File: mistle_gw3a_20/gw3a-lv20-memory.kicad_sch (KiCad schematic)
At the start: 9 parts, among them U13 MT48LC16M16A2TG, U6 W25Q128JVS

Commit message: Update gw3a dev board
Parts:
- added D6, D7: green, LED_SMD:LED_0805_2012Metric, symbol Device:LED
- added R13, R14, R35: 330, Resistor_SMD:R_0402_1005Metric, symbol Device:R_Small
- added R15, R16, R34: 1k, Resistor_SMD:R_0402_1005Metric, symbol Device:R_Small
- added R52, R57: 560, Resistor_SMD:R_0402_1005Metric, symbol Device:R_Small
- added SW2, SW5: KEY1, Button_Switch_SMD:SW_SPST_TL3342, symbol Switch:SW_Push
- added SW3: KEY2, Button_Switch_SMD:SW_SPST_TL3342, symbol Switch:SW_Push
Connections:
- net +3.3V: now also R13.1, R14.1, R35.1
- net DONE: now also R52.1
- net GND: now also D6.1 (K), D7.1 (K), R15.2, R16.2, R34.2
- net MODE[0..1]: no longer U7.21 (IOB52A/MODE1), U7.29 (IOB62B/MODE0)
- net READY: now also R57.1
- net ~{RESET}: now also R34.1, SW5.2
- net A0 renamed SDR_A0
- net A1 renamed SDR_A1
- net A2 renamed SDR_A2
- new net: R13.2, SW2.1
- new net: D6.2 (A), R52.2
- new net: D7.2 (A), R57.2
- new net: R35.2, SW5.1
- new net: R14.2, SW3.1
- new net MODE0: R15.1, SW2.2, U7.29 (IOB62B/MODE0)
- new net MODE1: R16.1, SW3.2, U7.21 (IOB52A/MODE1)
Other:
- moved on the sheet: C27, R29, R30, R31, R32, R59, U13, U6

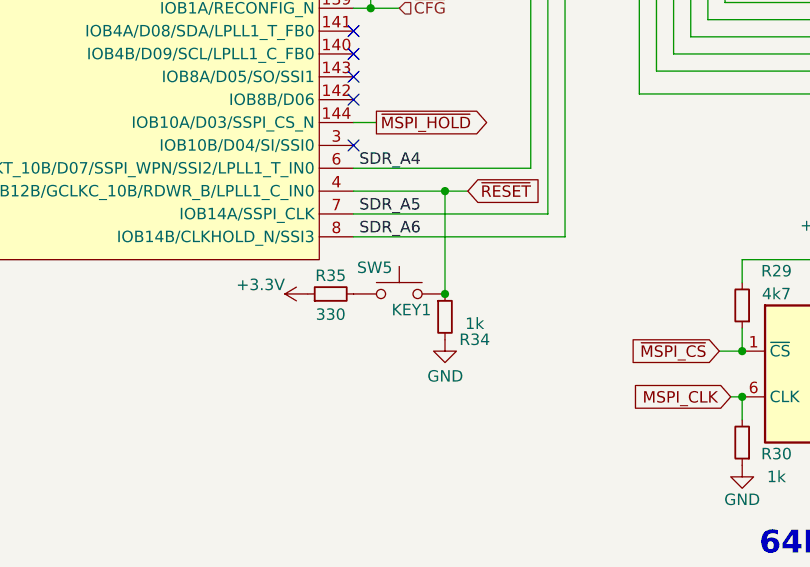
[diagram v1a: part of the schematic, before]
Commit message: Update gw3a 20 dev board
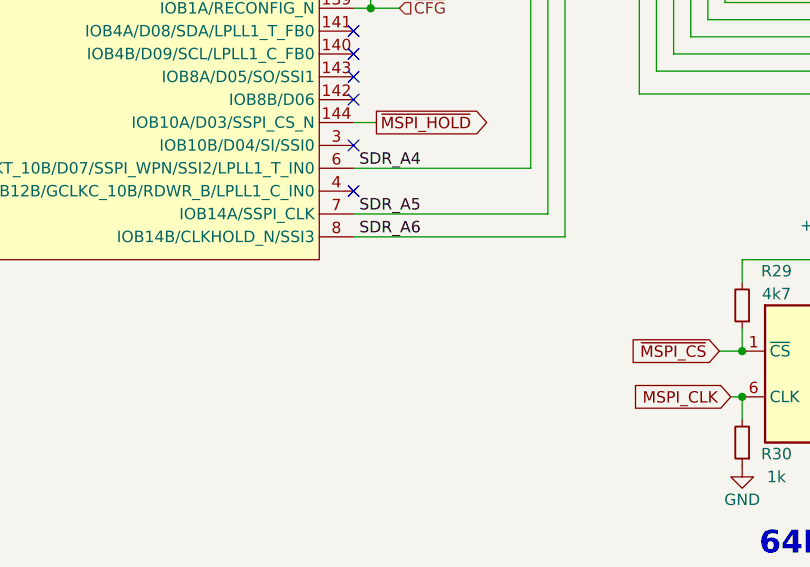
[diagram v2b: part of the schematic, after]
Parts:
- removed R34: 1k, Resistor_SMD:R_0402_1005Metric, symbol Device:R_Small
- removed R35: 330, Resistor_SMD:R_0402_1005Metric, symbol Device:R_Small
- removed SW5: KEY1, Button_Switch_SMD:SW_SPST_TL3342, symbol Switch:SW_Push
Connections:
- net ~{RESET}: no longer names the net of U7.4 (IOB12B/GCLKC_10B/RDWR_B/LPLL1_C_IN0)
- no-connect marks 5 -> 6

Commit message: Update gw3a dev board
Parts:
- C27, D6, D7, R13, R14, R15, R16, R29, R30, R31, R32, R52, R57, R59, SW2, SW3: checked once -> (none)
- U13: FT Rotation Offset (none) -> 270
- U6: value W25Q128JVS -> W25Q64JVS; LCSC Part # C131025 -> C179171; checked once -> (none)
- U7: value (none) -> GW3A-LV20-Q144
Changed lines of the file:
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@@
 		(in_pos_files yes)
 		(dnp no)
-		(fields_autoplaced yes)
 		(property "Reference" "U7"
 			(at -11.176 39.624 0)
@@
 			)
 		)
-		(property "Value" ""
-			(at 31.75 68.58 0)
+		(property "Value" "GW3A-LV20-Q144"
+			(at 24.638 91.694 0)
 			(show_name no)
 			(do_not_autoplace no)
@@
 			)
 		)
-		(property "checked" "once"
-			(at 118.745 174.625 0)
-			(hide yes)
-			(show_name no)
-			(do_not_autoplace no)
-			(effects
-				(font
-					(size 1.27 1.27)
-				)
-			)
-		)
 		(property "LCSC Part #" "C11702"
 			(at 118.745 174.625 0)
@@
 			)
 		)
-		(property "checked" "once"
-			(at 55.88 98.425 0)
-			(hide yes)
-			(show_name no)
-			(do_not_autoplace no)
-			(effects
-				(font
-					(size 1.27 1.27)
-				)
-			)
-		)
 		(property "LCSC Part #" "C11702"
 			(at 55.88 98.425 0)
@@
 		(in_pos_files yes)
 		(dnp no)
-		(fields_autoplaced yes)
 		(property "Reference" "U7"
 			(at 2.159 169.291 0)
@@
 			)
 		)
-		(property "Value" ""
-			(at 45.085 140.335 0)
+		(property "Value" "GW3A-LV20-Q144"
+			(at 26.67 155.956 0)
 			(show_name no)
 			(do_not_autoplace no)
@@
 			)
 		)
-		(property "checked" "once"
-			(at 50.8 95.885 0)
-			(hide yes)
-			(show_name no)
-			(do_not_autoplace no)
-			(effects
-				(font
-					(size 1.27 1.27)
-				)
-			)
-		)
 		(property "LCSC Part #" "C318884"
 			(at 50.8 95.885 0)
@@
 			)
 		)
-		(property "checked" "once"
-			(at 93.98 43.815 0)
-			(hide yes)
-			(show_name no)
-			(do_not_autoplace no)
-			(effects
-				(font
-					(size 1.27 1.27)
-				)
-			)
-		)
 		(property "LCSC Part #" "C2297"
 			(at 93.98 43.815 0)
@@
 			)
 		)
-		(property "checked" "once"
-			(at 87.63 50.8 90)
-			(hide yes)
-			(show_name no)
-			(do_not_autoplace no)
-			(effects
-				(font
-					(size 1.27 1.27)
-				)
-			)
-		)
 		(property "LCSC Part #" "C163460"
 			(at 87.63 50.8 90)
@@
 			)
 		)
-		(property "checked" "once"
-			(at 87.63 43.815 90)
-			(hide yes)
-			(show_name no)
-			(do_not_autoplace no)
-			(effects
-				(font
-					(size 1.27 1.27)
-				)
-			)
-		)
 		(property "LCSC Part #" "C163460"
 			(at 87.63 43.815 90)
@@
 			)
 		)
-		(property "checked" "once"
-			(at 118.745 159.385 0)
-			(hide yes)
-			(show_name no)
-			(do_not_autoplace no)
-			(effects
-				(font
-					(size 1.27 1.27)
-				)
-			)
-		)
 		(property "LCSC Part #" "C25900"
 			(at 118.745 159.385 0)
@@
 			)
 		)
-		(property "checked" "once"
-			(at 145.415 156.845 0)
-			(hide yes)
-			(show_name no)
-			(do_not_autoplace no)
-			(effects
-				(font
-					(size 1.27 1.27)
-				)
-			)
-		)
 		(property "LCSC Part #" "C25900"
 			(at 145.415 156.845 0)
@@
 		(in_pos_files yes)
 		(dnp no)
-		(fields_autoplaced yes)
 		(property "Reference" "U7"
 			(at 296.926 136.906 0)
@@
 			)
 		)
-		(property "Value" ""
-			(at 254 107.95 0)
+		(property "Value" "GW3A-LV20-Q144"
+			(at 237.998 140.462 0)
 			(show_name no)
 			(do_not_autoplace no)
@@
 			)
 		)
-		(property "checked" "once"
-			(at 93.98 50.8 0)
-			(hide yes)
-			(show_name no)
-			(do_not_autoplace no)
-			(effects
-				(font
-					(size 1.27 1.27)
-				)
-			)
-		)
 		(property "LCSC Part #" "C2297"
 			(at 93.98 50.8 0)
@@
 			)
 		)
-		(property "checked" "once"
-			(at 50.8 111.125 0)
-			(hide yes)
-			(show_name no)
-			(do_not_autoplace no)
-			(effects
-				(font
-					(size 1.27 1.27)
-				)
-			)
-		)
 		(property "LCSC Part #" "C318884"
 			(at 50.8 111.125 0)
@@
 			)
 		)
-		(property "checked" "once"
-			(at 154.305 154.305 90)
-			(hide yes)
-			(show_name no)
-			(do_not_autoplace no)
-			(effects
-				(font
-					(size 1.27 1.27)
-				)
-			)
-		)
 		(property "LCSC Part #" "C1525"
 			(at 154.305 154.305 90)
@@
 			)
 		)
-		(property "checked" "once"
-			(at 147.955 156.845 0)
-			(hide yes)
-			(show_name no)
-			(do_not_autoplace no)
-			(effects
-				(font
-					(size 1.27 1.27)
-				)
-			)
-		)
 		(property "LCSC Part #" "C25900"
 			(at 147.955 156.845 0)
@@
 			)
 		)
-		(property "checked" "once"
-			(at 77.47 122.555 90)
-			(hide yes)
-			(show_name no)
-			(do_not_autoplace no)
-			(effects
-				(font
-					(size 1.27 1.27)
-				)
-			)
-		)
 		(property "LCSC Part #" "C25900"
 			(at 77.47 122.555 90)
@@
 			)
 		)
+		(property "FT Rotation Offset" "270"
+			(at 140.335 85.09 0)
+			(hide yes)
+			(show_name no)
+			(do_not_autoplace no)
+			(effects
+				(font
+					(size 1.27 1.27)
+				)
+			)
+		)
 		(pin "10"
 		)
@@
 			)
 		)
-		(property "Value" "W25Q128JVS"
+		(property "Value" "W25Q64JVS"
 			(at 140.335 179.705 0)
 			(show_name no)
@@
 			)
 		)
-		(property "checked" "once"
-			(at 131.445 167.005 0)
-			(hide yes)
-			(show_name no)
-			(do_not_autoplace no)
-			(effects
-				(font
-					(size 1.27 1.27)
-				)
-			)
-		)
-		(property "LCSC Part #" "C131025"
+		(property "LCSC Part #" "C179171"
 			(at 131.445 167.005 0)
 			(hide yes)
@@
 			)
 		)
-		(property "checked" "once"
-			(at 43.18 111.125 90)
-			(hide yes)
-			(show_name no)
-			(do_not_autoplace no)
-			(effects
-				(font
-					(size 1.27 1.27)
-				)
-			)
-		)
 		(property "LCSC Part #" "C105875"
 			(at 43.18 111.125 90)
@@
 			)
 		)
-		(property "checked" "once"
-			(at 43.18 95.885 90)
-			(hide yes)
-			(show_name no)
-			(do_not_autoplace no)
-			(effects
-				(font
-					(size 1.27 1.27)
-				)
-			)
-		)
 		(property "LCSC Part #" "C105875"
 			(at 43.18 95.885 90)
@@
 			)
 		)
-		(property "Value" ""
-			(at 51.435 36.195 0)
+		(property "Value" "GW3A-LV20-Q144"
+			(at 49.53 42.672 0)
 			(show_name no)
 			(do_not_autoplace no)
@@
 			(at 55.88 113.665 0)
 			(hide yes)
-			(show_name no)
-			(do_not_autoplace no)
-			(effects
-				(font
-					(size 1.27 1.27)
-				)
-			)
-		)
-		(property "checked" "once"
-			(at 55.88 113.665 0)
-			(hide yes)

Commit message: Update gw3a board
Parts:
- removed D7: green, LED_SMD:LED_0805_2012Metric, symbol Device:LED
- removed R52, R57: 560, Resistor_SMD:R_0402_1005Metric, symbol Device:R_Small
- added R61, R62: 4k7, Resistor_SMD:R_0402_1005Metric, symbol Device:R_Small
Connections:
- net +3.3V: now also R61.1, R62.1
- net DONE: now also D6.2 (A), R62.2
- net READY: now also R61.2
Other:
- moved on the sheet: D6
